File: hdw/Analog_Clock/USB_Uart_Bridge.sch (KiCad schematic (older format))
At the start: 31 parts

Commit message: More schematic work
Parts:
- removed C?: 0.1uF, Capacitors_SMD:C_0402, symbol Custom_Library:C_Custom
- removed TP?: TP, Pin_Headers:Pin_Header_Angled_1x01_Pitch2.54mm, symbol Custom_Library:TP
- added R? (x2): 10k, Resistors_SMD:R_0402, symbol Custom_Library:R_Custom
- C? (x2): display_footprint (none) -> 0402
- C?: footprint Capacitors_SMD:C_0805 -> Capacitors_SMD:C_0603; Dielectric X7R -> X5R; Digi-Key PN 1276-2970-1-ND -> 490-16348-1-ND; Voltage 16V -> 10V; display_footprint 0805 -> 0603
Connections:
- net labels added: +3.3V, GND, USB_UART_RX, USB_UART_TX
- net labels removed: GND_USB, USB_UART_RX_ISO, USB_UART_TX_ISO
- wire segments 52 -> 57
- no-connect marks 3 -> 4
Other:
- note removed: "11. USB UART Bridge"
- moved on the sheet: R?

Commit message: a few sch adjustments
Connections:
- wire segments 57 -> 65
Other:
- note added: "ADD LEVEL SHIFTER/TRISTATE BUFFER STUFF"

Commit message: More sch work
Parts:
- added C? (x2): 0.1uF, Capacitors_SMD:C_0402, symbol Custom_Library:C_Custom
- added R? (x2): 10k, Resistors_SMD:R_0402, symbol Custom_Library:R_Custom
- added U? (x2): 74LVC1G07, TO_SOT_Packages_SMD:SOT-353_SC-70-5, symbol Custom_Library:74LVC1G07_Power
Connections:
- net labels added: +3.3V_USB, USB_UART_RX_BUF, USB_UART_TX_BUF
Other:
- moved on the sheet: C?, D?, J?, L?, R?, TP?, U?

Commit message: more analog work, added some more sch stuff
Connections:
- net +3V3: now also C?.1
- net +5V_USB: no longer C?.1
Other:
- note removed: "ADD LEVEL SHIFTER/TRISTATE BUFFER STUFF"
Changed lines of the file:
@@
 $Descr A 11000 8500
 encoding utf-8
-Sheet 13 23
+Sheet 13 24
 Title "VFD Clock"
 Date "2019-04-11"
@@
 	-1   0    0    -1
 $EndComp
-$Comp
-L Custom_Library:+5V_USB #PWR?
-U 1 1 5C037C4F
-P 3540 7400
-F 0 "#PWR?" H 3540 7250 50  0001 C CNN
-F 1 "+5V_USB" H 3540 7540 50  0000 C CNN
-F 2 "" H 3540 7400 50  0001 C CNN
-F 3 "" H 3540 7400 50  0001 C CNN
-	1    3540 7400
-	1    0    0    -1
-$EndComp
 Wire Wire Line
 	5730 3840 6980 3840
@@
 Wire Wire Line
 	8580 2670 7900 2670
-Text Notes 770  4270 0    50   ~ 0
-ADD LEVEL SHIFTER/TRISTATE BUFFER STUFF
 $Comp
 L power:GND #PWR?
@@
 	1    0    0    -1
 $EndComp
+$Comp
+L power:+3.3V #PWR?
+U 1 1 5F35E4BA
+P 3540 7400
+F 0 "#PWR?" H 3540 7250 50  0001 C CNN
+F 1 "+3.3V" H 3540 7540 50  0000 C CNN
+F 2 "" H 3540 7400 50  0001 C CNN
+F 3 "" H 3540 7400 50  0001 C CNN
+	1    3540 7400
+	1    0    0    -1
+$EndComp

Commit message: big sch push
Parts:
- removed C?: 4.7uF, Capacitors_SMD:C_0603, symbol Custom_Library:C_Custom
- added C1306: 10uF, Capacitors_SMD:C_0805, symbol Custom_Library:C_Custom
- C1301, C1302, C1303, C1304, C1305, C1307, C1308, C1311: renamed from C?; footprint Capacitors_SMD:C_0402 -> Capacitors_SMD:C_0603; Digi-Key PN 490-10701-1-ND -> 399-7845-1-ND; display_footprint 0402 -> 0603
- C1309, C1310: renamed from C?; footprint (none) -> Capacitors_SMD:C_0603; Digi-Key PN (none) -> 399-7918-1-ND; display_footprint 0402 -> 0603
- D1301: renamed from D?; footprint (none) -> LEDs:LED_0603; Digi-Key PN (none) -> 754-1124-1-ND
- L1301, L1302: renamed from L?; Digi-Key PN 732-2389-1-ND -> 732-1593-1-ND
- R1301, R1302, R1306, R1307, R1308, R1315: renamed from R?; footprint Resistors_SMD:R_0402 -> Resistors_SMD:R_0603; Digi-Key PN RMCF0402FT10K0CT-ND -> (none); Wattage 1/16W -> 1/10W; display_footprint 0402 -> 0603
- R1303, R1304, R1305, R1309, R1311, R1312, R1313: renamed from R?; footprint Resistors_SMD:R_0402 -> Resistors_SMD:R_0603; Wattage 1/16W -> 1/10W; display_footprint 0402 -> 0603
- R1314: renamed from R?; footprint Resistors_SMD:R_0402 -> Resistors_SMD:R_0603; Digi-Key PN 541-1.00KLCT-ND -> (none); Wattage 1/16W -> 1/10W; display_footprint 0402 -> 0603
- gave numbers to parts that had none: 9
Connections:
- net +5V_USB: now also C1306.1
- net GND: now also C1306.2

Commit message: Much more schematic progress
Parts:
- removed C1301, C1302: 0.1uF, Capacitors_SMD:C_0603, symbol Custom_Library:C_Custom
- removed R1301, R1302: 10k, Resistors_SMD:R_0603, symbol Custom_Library:R_Custom
- removed U1301, U1302: 74LVC1G07, TO_SOT_Packages_SMD:SOT-353_SC-70-5, symbol Custom_Library:74LVC1G07_Power
- added C1305, C1310, C1312: 0.1uF, Capacitors_SMD:C_0603, symbol Custom_Library:C_Custom
- added C1308: 10uF, Capacitors_SMD:C_0603, symbol Custom_Library:C_Custom
- added R1308, R1314, R1315: 100k, Resistors_SMD:R_0603, symbol Custom_Library:R_Custom
- added U1303: 74LVC1G17, TO_SOT_Packages_SMD:SOT-353_SC-70-5, symbol Custom_Library:74LVC1G17_Power
- added U1304: TXB0102DCU, Package_SO:VSSOP-8_2.4x2.1mm_P0.5mm, symbol Logic_LevelTranslator:TXB0102DCU
- R1301: renamed from R1314; Digi-Key PN (none) -> 311-1.00KHRCT-ND
- R1302: renamed from R1303; Digi-Key PN (none) -> 311-487KHRCT-ND
- R1303: renamed from R1304; Digi-Key PN (none) -> RMCF0603FT6K04CT-ND
- R1304: renamed from R1305; Digi-Key PN (none) -> RMCF0603FT40K2CT-ND
- R1305: renamed from R1308; Digi-Key PN (none) -> YAG2321CT-ND
- R1306: value 10k -> 100k; Digi-Key PN (none) -> RMCF0603FT100KCT-ND
- R1307: value 10k -> 1k; Digi-Key PN (none) -> 311-1.00KHRCT-ND
- R1309, R1313: Digi-Key PN (none) -> YAG2321CT-ND
- R1311, R1312: Digi-Key PN (none) -> 311-27.0HRCT-ND
- R1316: renamed from R1315; Digi-Key PN (none) -> YAG2321CT-ND
- renumbered C1303 to C1301, C1305 to C1302, C1306 to C1303, C1307 to C1306, C1308 to C1307, C1310 to C1311, C1311 to C1313, U1303 to U1301, U1304 to U1302
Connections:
- net +3.3V_USB: now also C1312.1, R1314.1, R1315.1, U1304.7 (VCCB); no longer R1306.1, R1307.1
- net +3V3: now also R1306.1, C1305.1, C1310.1, R1308.1, U1303.5 (VCC), U1304.3 (VCCA)
- net GND: now also C1305.2, C1308.2, C1310.2, C1312.2, U1303.3 (GND), U1304.2 (GND)
- net POS5_USB_PGOOD: now also U1303.2
- net USB_UART_RX: now also R1308.2, U1304.5 (A1)
- net USB_UART_RX_BUF: now also R1314.2, U1304.8 (B1); no longer R1306.2
- net USB_UART_TX: now also R1306.2, U1304.4 (A2)
- net USB_UART_TX_BUF: now also R1315.2, U1304.1 (B2); no longer R1307.2
- new net: C1308.1, R1307.1, U1304.6 (OE)
- new net: R1307.2, U1303.4
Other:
- moved on the sheet: C1301, C1302, C1303, C1304, C1306, C1307, C1309, C1311, C1313, D1301, J1301, L1301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

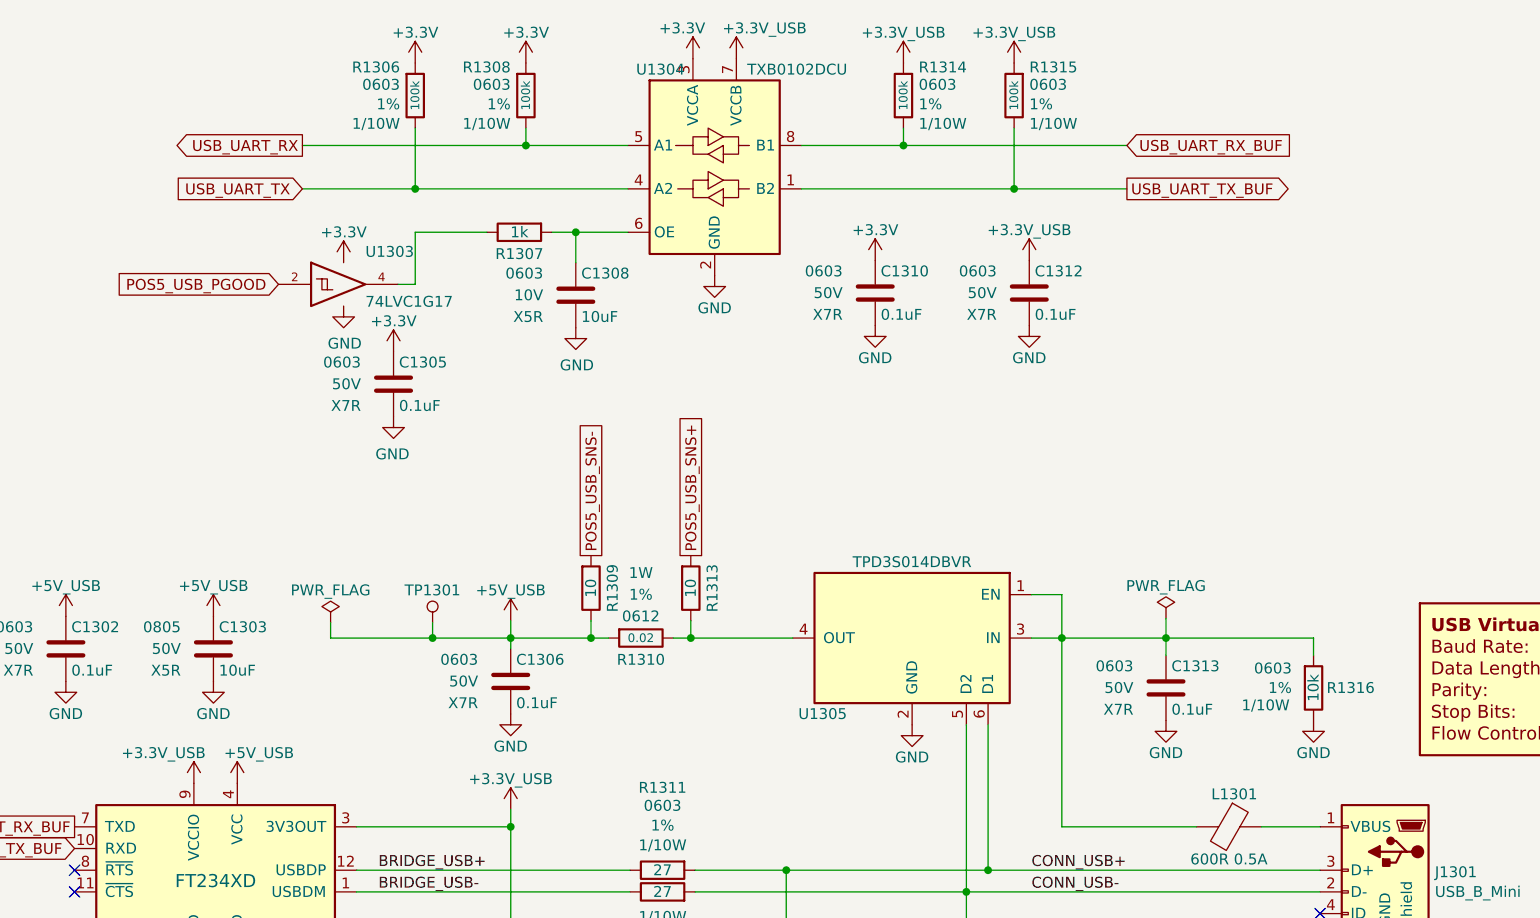
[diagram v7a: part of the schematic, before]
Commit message: Arranged more components on PCB
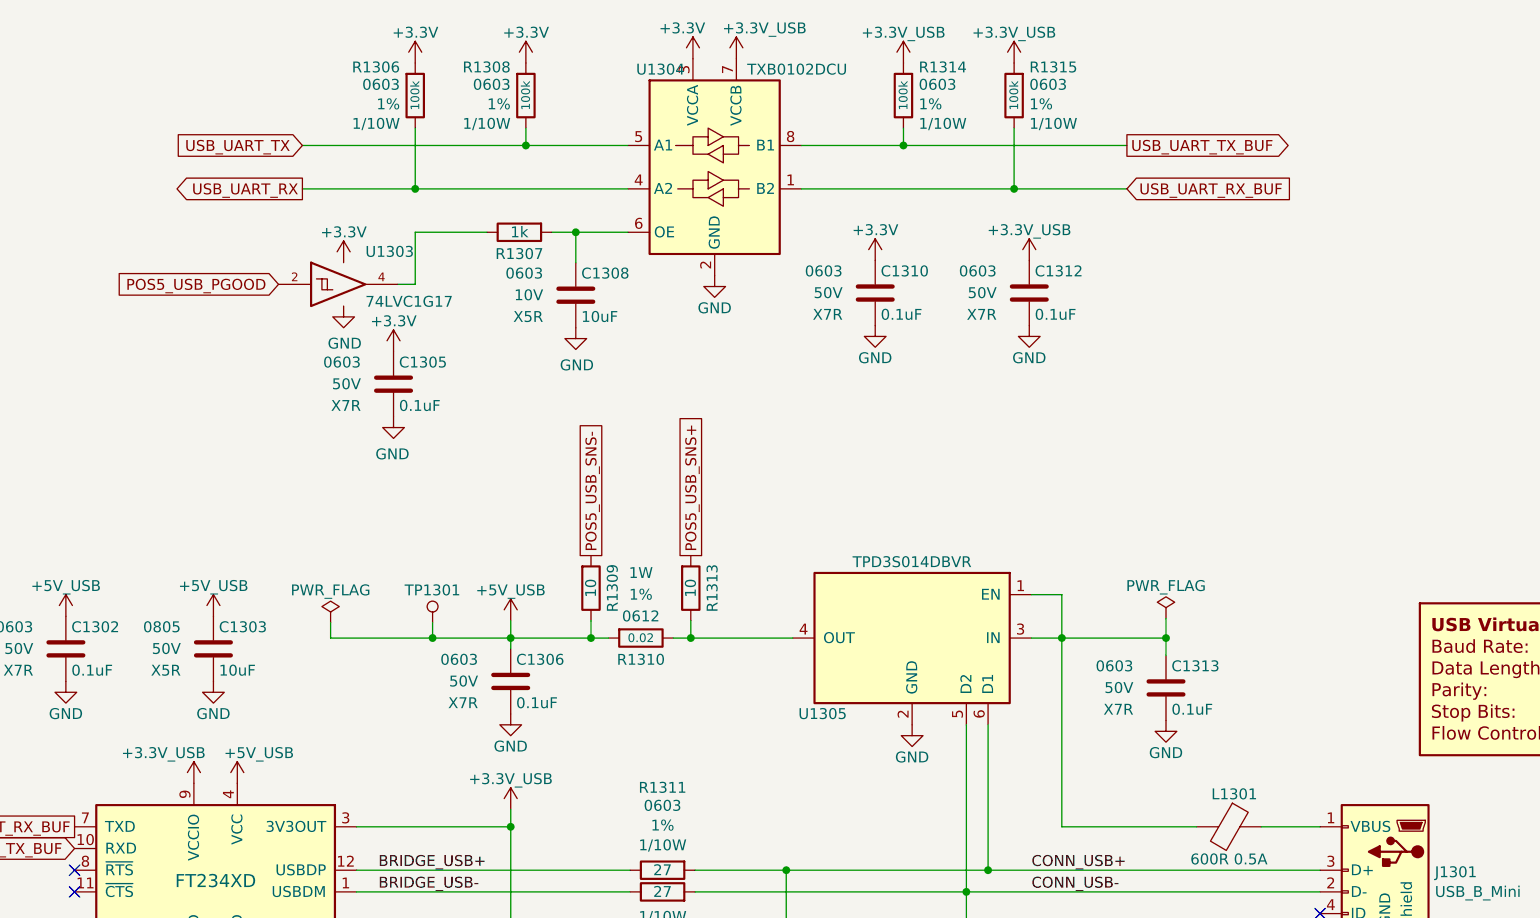
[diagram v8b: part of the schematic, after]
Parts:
- removed R1316: 10k, Resistors_SMD:R_0603, symbol Custom_Library:R_Custom
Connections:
- net USB_UART_RX: now also R1306.2, U1304.4 (A2); no longer R1308.2, U1304.5 (A1)
- net USB_UART_RX_BUF: now also R1315.2, U1304.1 (B2); no longer R1314.2, U1304.8 (B1)
- net USB_UART_TX: now also R1308.2, U1304.5 (A1); no longer R1306.2, U1304.4 (A2)
- net USB_UART_TX_BUF: now also R1314.2, U1304.8 (B1); no longer R1315.2, U1304.1 (B2)
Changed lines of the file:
@@
 $EndComp
-$Comp
-L Custom_Library:R_Custom R1316
-U 1 1 5E9C0D8F
-P 8110 3860
-F 0 "R1316" H 8050 3860 50  0000 R CNN
-F 1 "10k" V 8110 3860 50  0000 C CNN
-F 2 "Resistors_SMD:R_0603" H 8110 3860 50  0001 C CNN
-F 3 "" H 8110 3860 50  0001 C CNN
-F 4 "0603" H 8210 3950 50  0000 L CNN "display_footprint"
-F 5 "1%" H 8210 3860 50  0000 L CNN "Tolerance"
-F 6 "1/10W" H 8220 3780 50  0000 L CNN "Wattage"
-F 7 "YAG2321CT-ND" H 8410 4260 60  0001 C CNN "Digi-Key PN"
-	1    8110 3860
-	-1   0    0    -1
-$EndComp
-$Comp
-L power:GND #PWR01343
-U 1 1 5E9C26CC
-P 8110 4010
-F 0 "#PWR01343" H 8110 3760 50  0001 C CNN
-F 1 "GND" H 8110 3860 50  0000 C CNN
-F 2 "" H 8110 4010 50  0001 C CNN
-F 3 "" H 8110 4010 50  0001 C CNN
-	1    8110 4010
-	1    0    0    -1
-$EndComp
-Wire Wire Line
-	8110 3710 8110 3630
-Wire Wire Line
-	8110 3630 7430 3630
 $Comp
 L power:GND #PWR01325
@@
 	1    0    0    -1
 $EndComp
-Text GLabel 7250 1360 2    50   Input ~ 0
-USB_UART_RX_BUF
-Text GLabel 7250 1560 2    50   Output ~ 0
-USB_UART_TX_BUF
 $Comp
 L Custom_Library:+3.3V_USB #PWR01336
@@
 Wire Wire Line
 	6730 1560 5750 1560
-Text GLabel 3450 1360 0    50   Output ~ 0
+Text GLabel 3450 1560 0    50   Output ~ 0
 USB_UART_RX
-Text GLabel 3450 1560 0    50   Input ~ 0
+Text GLabel 3450 1360 0    50   Input ~ 0
 USB_UART_TX
 $Comp
@@
 Wire Wire Line
 	3970 1760 4300 1760
+Text GLabel 7250 1360 2    50   Output ~ 0
+USB_UART_TX_BUF
+Text GLabel 7250 1560 2    50   Input ~ 0
+USB_UART_RX_BUF
 $EndSCHEMATC
